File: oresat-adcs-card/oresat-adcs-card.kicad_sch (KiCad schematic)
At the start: 0 parts

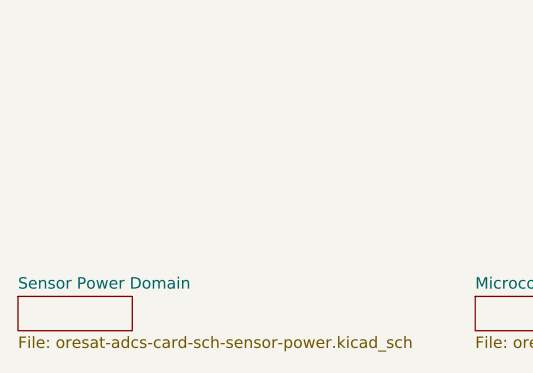
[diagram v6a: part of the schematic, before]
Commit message: Design review changes
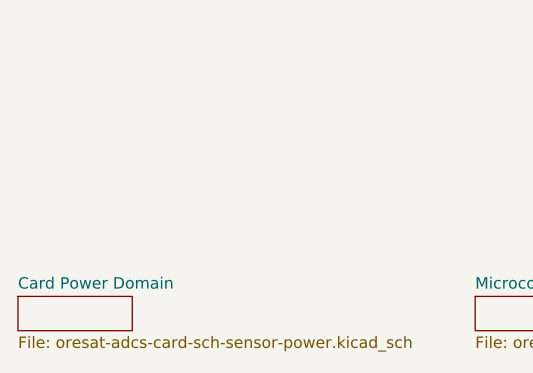
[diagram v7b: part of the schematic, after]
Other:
- sheet Sensor Power Domain renamed Card Power Domain
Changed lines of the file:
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@@
     (stroke (width 0) (type solid))
     (fill (color 0 0 0 0.0000))
-    (property "Sheetname" "Sensor Power Domain" (at 25.4 75.4884 0)
+    (property "Sheetname" "Card Power Domain" (at 25.4 75.4884 0)
       (effects (font (size 1.27 1.27)) (justify left bottom))
     )
@@
     (instances
       (project "oresat-adcs-card"
-        (path "/c58960d9-4cac-4036-ad2e-1aef26946dae" (page "#"))
+        (path "/c58960d9-4cac-4036-ad2e-1aef26946dae" (page "2"))
       )
     )
@@
     (instances
       (project "oresat-adcs-card"
-        (path "/c58960d9-4cac-4036-ad2e-1aef26946dae" (page "#"))
+        (path "/c58960d9-4cac-4036-ad2e-1aef26946dae" (page "1"))
       )
     )
@@
     (instances
       (project "oresat-adcs-card"
-        (path "/c58960d9-4cac-4036-ad2e-1aef26946dae" (page "#"))
+        (path "/c58960d9-4cac-4036-ad2e-1aef26946dae" (page "6"))
       )
     )
@@
     (instances
       (project "oresat-adcs-card"
-        (path "/c58960d9-4cac-4036-ad2e-1aef26946dae" (page "#"))
+        (path "/c58960d9-4cac-4036-ad2e-1aef26946dae" (page "8"))
       )
     )
@@
     (instances
       (project "oresat-adcs-card"
-        (path "/c58960d9-4cac-4036-ad2e-1aef26946dae" (page "#"))
+        (path "/c58960d9-4cac-4036-ad2e-1aef26946dae" (page "5"))
       )
     )
@@
     (instances
       (project "oresat-adcs-card"
-        (path "/c58960d9-4cac-4036-ad2e-1aef26946dae" (page "#"))
+        (path "/c58960d9-4cac-4036-ad2e-1aef26946dae" (page "7"))
       )
     )
@@
     (instances
       (project "oresat-adcs-card"
-        (path "/c58960d9-4cac-4036-ad2e-1aef26946dae" (page "10"))
+        (path "/c58960d9-4cac-4036-ad2e-1aef26946dae" (page "9"))
       )
     )
@@
     (instances
       (project "oresat-adcs-card"
-        (path "/c58960d9-4cac-4036-ad2e-1aef26946dae" (page "#"))
+        (path "/c58960d9-4cac-4036-ad2e-1aef26946dae" (page "3"))
       )
     )
@@
     (instances
       (project "oresat-adcs-card"
-        (path "/c58960d9-4cac-4036-ad2e-1aef26946dae" (page "#"))
+        (path "/c58960d9-4cac-4036-ad2e-1aef26946dae" (page "4"))
       )
     )
